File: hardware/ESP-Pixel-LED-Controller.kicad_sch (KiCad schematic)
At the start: 31 parts, among them J1 DMX_IN, J2 DMX_OUT, J3 12V INPUT, J4 5V INPUT, J5 FTDI, J6 I2C-Display, J7 LED-Stripe, Q1 BSS138, U1 TSR_1-2450, U2 ADM2483xRW, U3 LM809, U4 WT32-ETH-01

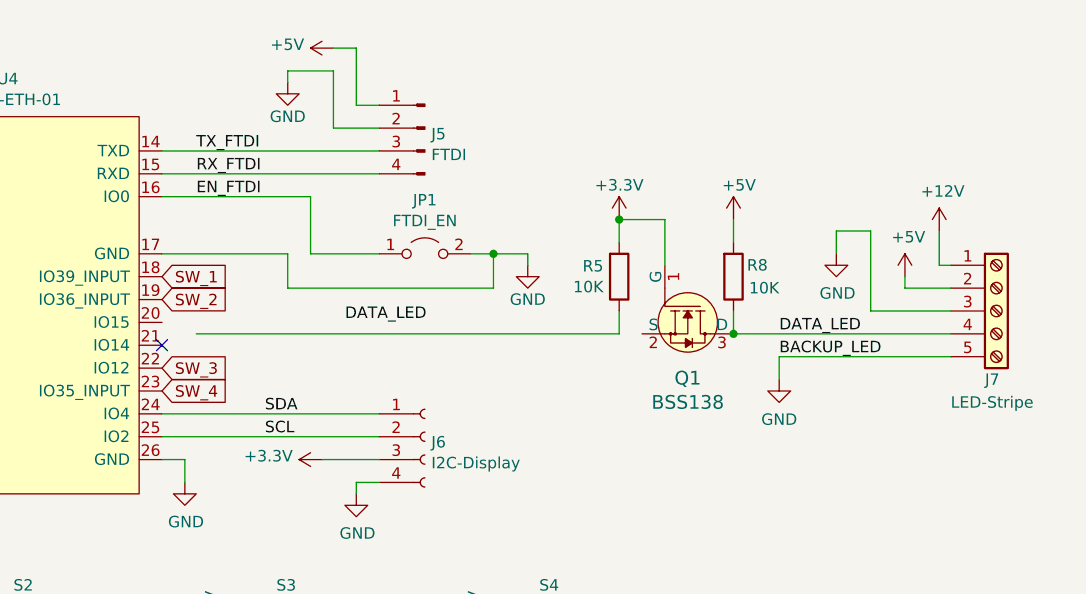
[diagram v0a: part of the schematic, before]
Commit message: 🐛✨ added missing connection
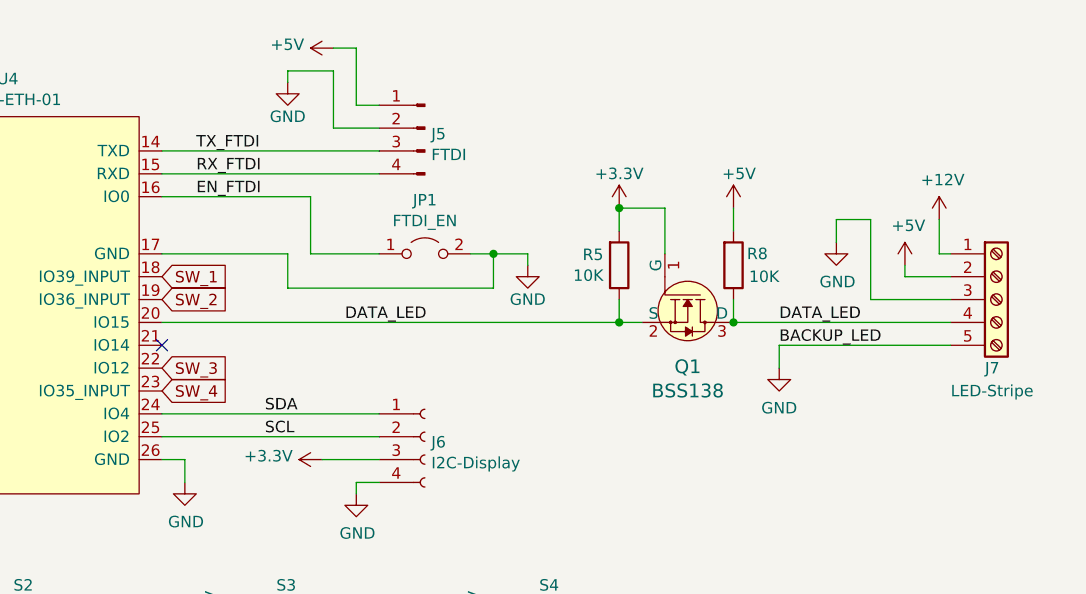
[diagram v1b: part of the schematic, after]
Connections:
- net DATA_LED: now also Q1.2 (S), R5.1, U4.20 (IO15~{})
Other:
- moved on the sheet: J7, Q1, R5, R8
